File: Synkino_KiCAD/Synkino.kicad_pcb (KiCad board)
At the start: 2 copper layers, 88.4 x 82.3 mm, 180 parts, among them J1 Conn_01x02_Male, J10 EYE8_OUT, J11 EYE4_OUT, J12 2.5mm, J13 EYE5_OUT, J2 2.5mm, J3 3.5mm, J4 Micro_SD_Card_Det_Hirose_DM3AT, J5 EYE1_OUT, J6 EYE6_OUT, J7 EYE2_OUT, J8 EYE7_OUT, J9 EYE3_OUT, Q1 IRF7319, Q2 BC847, SW1 SW_Push, SW2 Rotary_Encoder_Switch, SW3 SW_Push, U1 MCP1702T-5002E/MB, U10 ATMEGA328P-AU, U11 QRE1113, U12 QRE1113, U13 QRE1113, U14 QRE1113, U15 QRE1113, U16 QRE1113, U18 QRE1113, U2 ATMEGA328P-AU, U3 74HC4050, U4 SPIOLED128x64, U5 AP7312-1833W6-7, U6 74HC14, U7 VS1053B, U8 MAX4741, U9 QRE1113, X1 FTDIconn, X2 ICSP, X3 FTDIconn, X4 ICSP, Y1 16Mhz, Y2 12.288MHz, Y3 16Mhz

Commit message: Beautification
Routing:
- net GND: track 176.0 -> 174.2 mm
- net +5V: track 283.3 -> 282.3 mm
- net +3V3: track 220.5 -> 219.8 mm

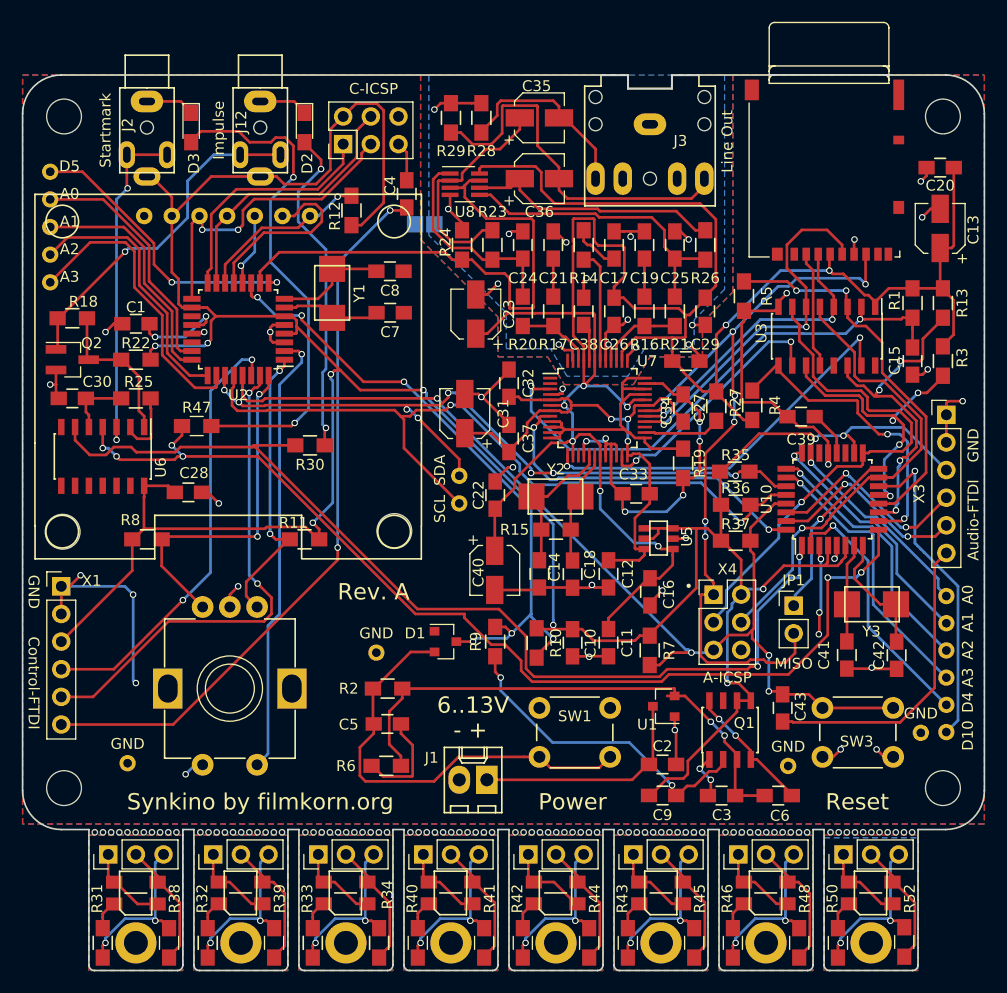
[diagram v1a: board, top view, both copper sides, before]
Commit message: Fixed the U1 footprint
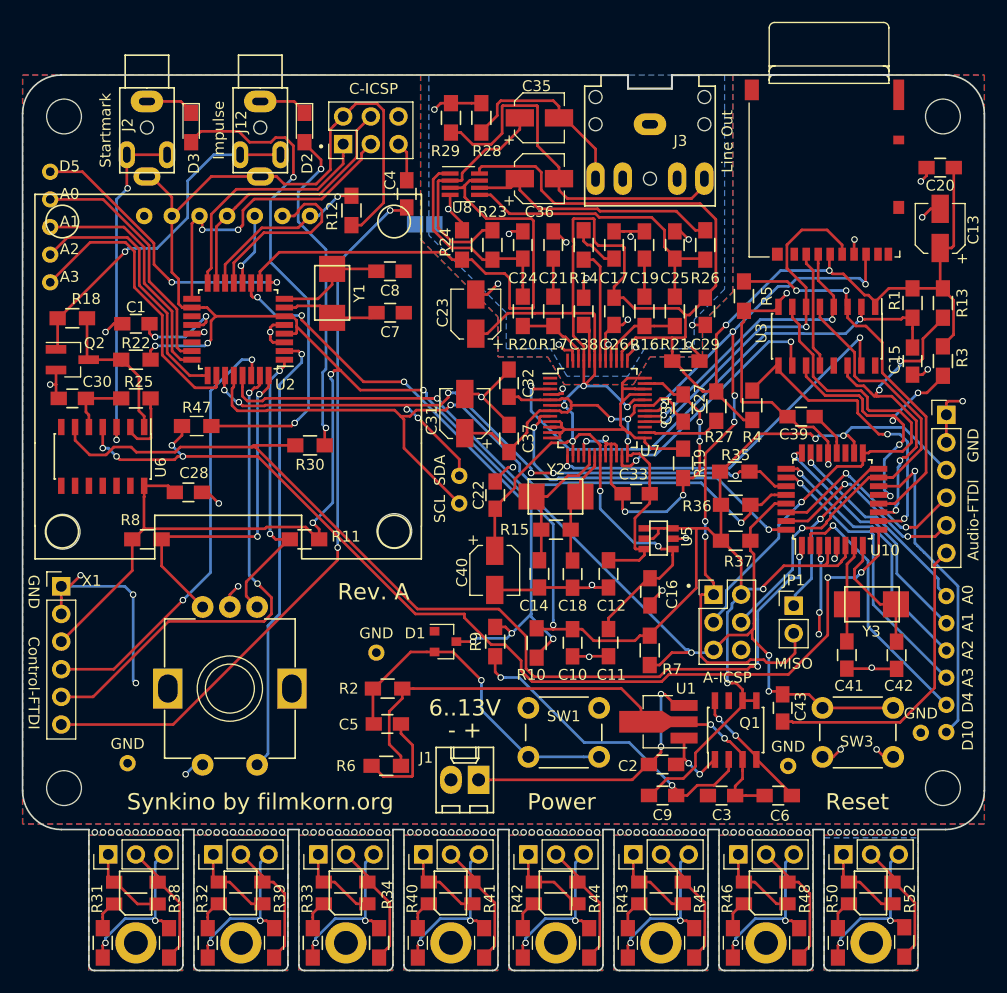
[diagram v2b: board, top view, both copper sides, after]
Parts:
- U1: footprint TO_SOT_Packages_SMD:SOT-23 -> TO_SOT_Packages_SMD:SOT-89-3_Handsoldering
- moved U1 1.43 mm to (130.4, 97.5)
- moved SW1 1.02 mm to (118.1, 96.3)
- moved J1 0.76 mm to (113.5, 102.9)
- moved Q1 0.51 mm to (137.2, 98.3)
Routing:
- net Net-(C5-Pad2): track 40.7 -> 31.2 mm, vias 0 -> 1
- net Net-(C2-Pad1): track 21.1 -> 25.7 mm, vias 0 -> 2
- net GND: track 174.2 -> 171.0 mm, vias 40 -> 39
- net Net-(C3-Pad2): track 49.3 -> 51.2 mm
- net Net-(C6-Pad1): track 12.7 -> 11.6 mm

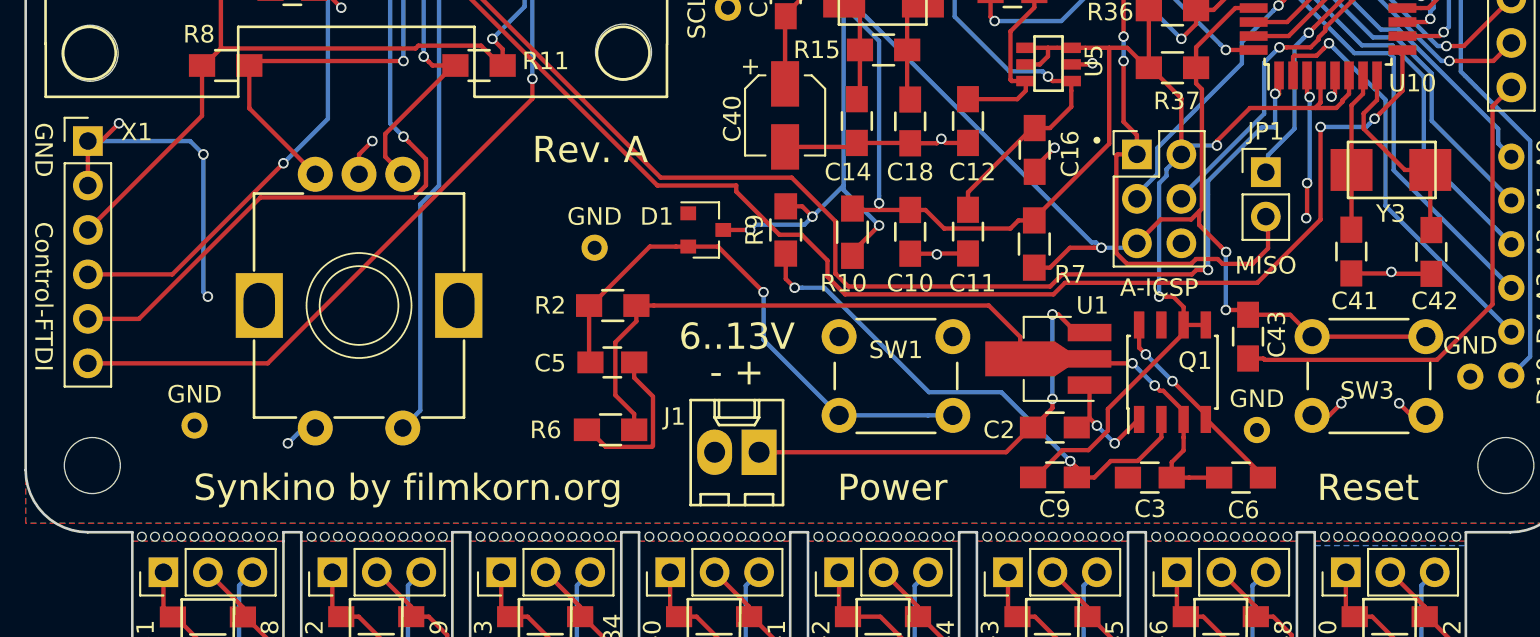
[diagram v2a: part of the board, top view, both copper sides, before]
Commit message: Making Power button bigger
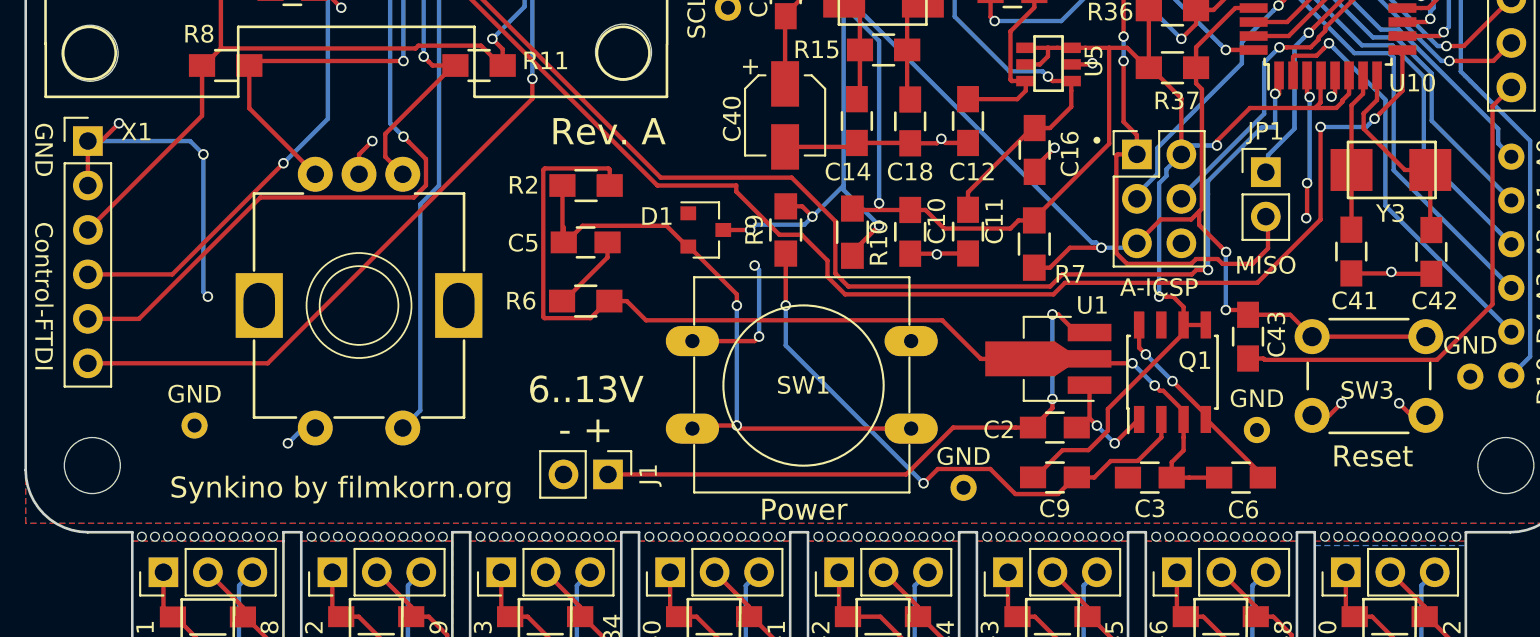
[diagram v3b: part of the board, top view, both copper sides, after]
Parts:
- J1: footprint Connectors_Molex:Molex_KK-6410-02_02x2.54mm_Straight -> Pin_Headers:Pin_Header_Straight_1x02_Pitch2.54mm
- SW1: footprint Buttons_Switches_THT:SW_PUSH_6mm_h5mm -> Buttons_Switches_THT:SW_PUSH-12mm
- moved GND 25.2 mm to (125.2, 104.9)
- moved J1 8.73 mm to (104.9, 104.1), turned to 270 degrees
- moved SW1 8.39 mm to (109.7, 96.5)
- moved R6 7.49 mm to (103.6, 94.2)
- moved C5 7.03 mm to (103.6, 90.9)
- moved R2 7.03 mm to (103.7, 87.6)
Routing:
- net Net-(C3-Pad2): track 51.2 -> 61.4 mm
- net Net-(C2-Pad1): track 25.7 -> 35.0 mm
- net GND: track 171.0 -> 179.1 mm, vias 39 -> 41
- net Net-(C5-Pad2): track 31.2 -> 36.2 mm, vias 1 -> 2
- net Net-(C5-Pad1): track 9.41 -> 4.59 mm
- net Net-(C9-Pad2): track 29.9 -> 33.3 mm

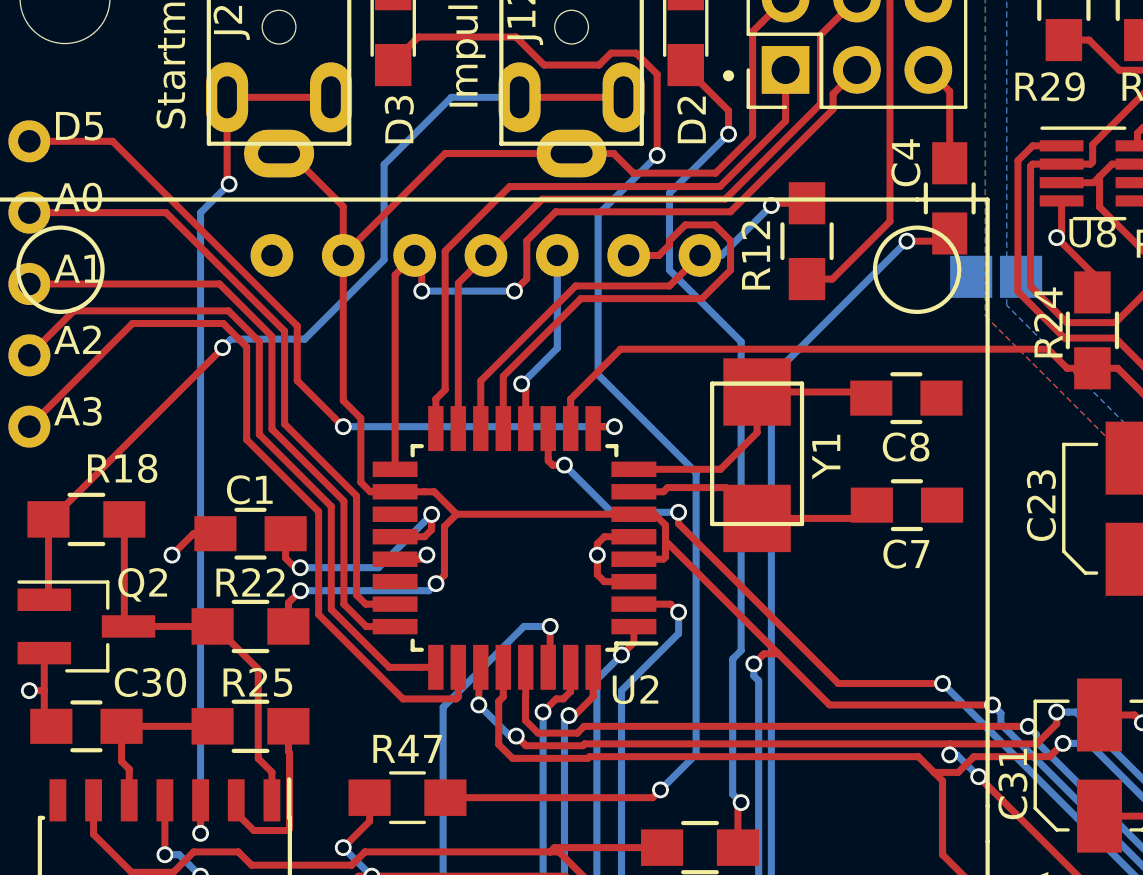
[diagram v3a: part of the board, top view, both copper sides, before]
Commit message: Bit more GND planes
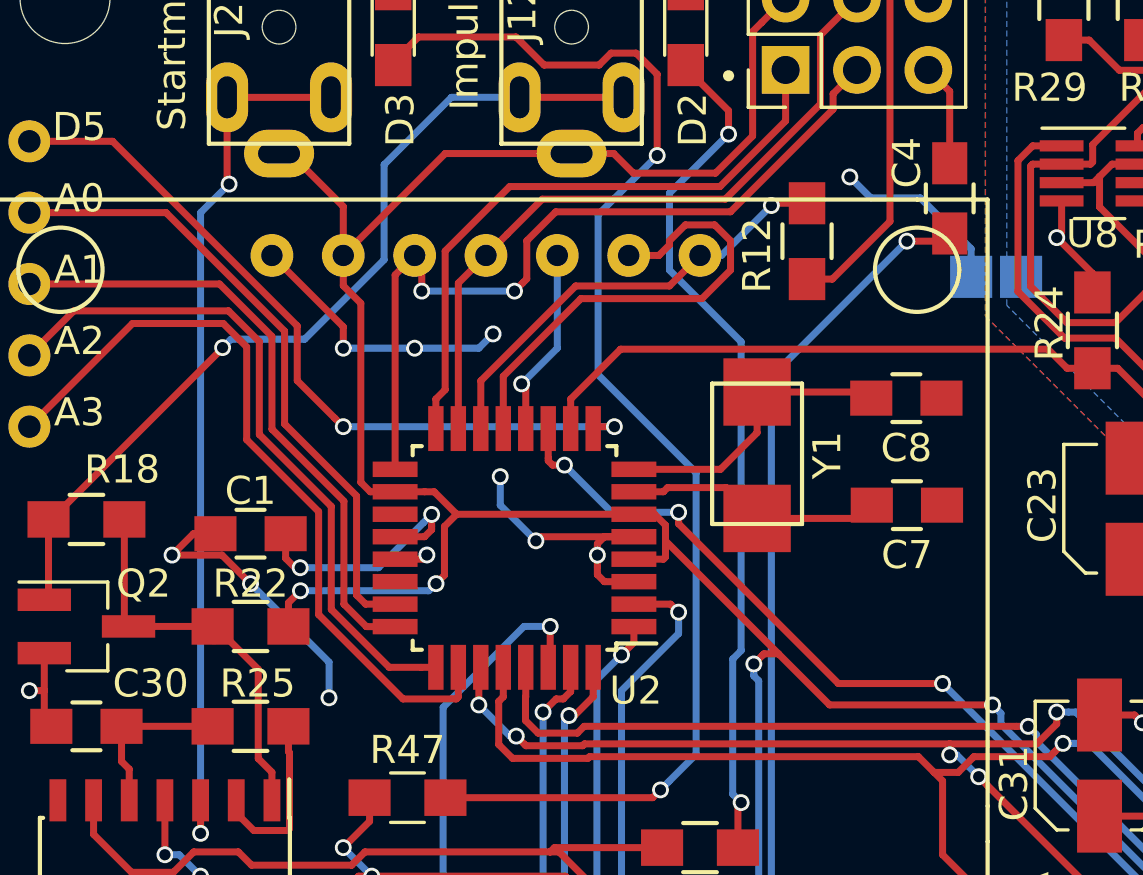
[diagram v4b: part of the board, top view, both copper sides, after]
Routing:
- net GND: track 179.1 -> 210.1 mm, vias 41 -> 49
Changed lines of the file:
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@@
     (links 370)
     (no_connects 0)
-    (area 71.552999 38.024999 160.095001 120.471001)
+    (area 62.682429 32.843999 168.838572 132.270286)
     (thickness 1.6)
     (drawings 81)
-    (tracks 2008)
+    (tracks 2033)
     (zones 0)
     (modules 180)
@@
   (segment (start 83.292 60.96) (end 83.292 61.835) (width 0.25) (layer F.Cu) (net 1))
   (via (at 83.81038 62.171306) (size 0.6) (drill 0.4) (layers F.Cu B.Cu) (net 1))
+  (segment (start 105.885792 49.005792) (end 104.123792 49.005792) (width 0.25) (layer B.Cu) (net 2))
+  (segment (start 104.123792 49.005792) (end 103.378 48.26) (width 0.25) (layer B.Cu) (net 2))
+  (via (at 103.378 48.26) (size 0.6) (drill 0.4) (layers F.Cu B.Cu) (net 2))
+  (segment (start 107.696 51.816) (end 107.696 50.816) (width 0.25) (layer B.Cu) (net 2))
+  (segment (start 107.696 50.816) (end 105.885792 49.005792) (width 0.25) (layer B.Cu) (net 2))
+  (segment (start 87.884 54.356) (end 90.17 54.356) (width 0.25) (layer B.Cu) (net 2))
+  (segment (start 90.17 54.356) (end 90.678 53.848) (width 0.25) (layer B.Cu) (net 2))
+  (via (at 90.678 53.848) (size 0.6) (drill 0.4) (layers F.Cu B.Cu) (net 2))
+  (segment (start 85.344 54.356) (end 87.884 54.356) (width 0.25) (layer B.Cu) (net 2))
+  (via (at 87.884 54.356) (size 0.6) (drill 0.4) (layers F.Cu B.Cu) (net 2))
+  (segment (start 85.344 53.594) (end 85.344 54.356) (width 0.25) (layer F.Cu) (net 2))
+  (segment (start 82.804 51.054) (end 85.344 53.594) (width 0.25) (layer F.Cu) (net 2))
+  (via (at 85.344 54.356) (size 0.6) (drill 0.4) (layers F.Cu B.Cu) (net 2))
+  (segment (start 92.202 61.214) (end 90.932 59.944) (width 0.25) (layer B.Cu) (net 2))
+  (segment (start 90.932 59.944) (end 90.932 58.928) (width 0.25) (layer B.Cu) (net 2))
+  (via (at 90.932 58.928) (size 0.6) (drill 0.4) (layers F.Cu B.Cu) (net 2))
+  (segment (start 95.69 61.068) (end 92.348 61.068) (width 0.25) (layer F.Cu) (net 2))
+  (segment (start 92.348 61.068) (end 92.202 61.214) (width 0.25) (layer F.Cu) (net 2))
+  (via (at 92.202 61.214) (size 0.6) (drill 0.4) (layers F.Cu B.Cu) (net 2))
+  (segment (start 82.042 62.738) (end 84.836 65.532) (width 0.25) (layer B.Cu) (net 2))
+  (via (at 84.836 66.802) (size 0.6) (drill 0.4) (layers F.Cu B.Cu) (net 2))
+  (segment (start 84.836 65.532) (end 84.836 66.802) (width 0.25) (layer B.Cu) (net 2))
+  (segment (start 79.248 61.722) (end 81.026 61.722) (width 0.25) (layer F.Cu) (net 2))
+  (segment (start 81.026 61.722) (end 82.042 62.738) (width 0.25) (layer F.Cu) (net 2))
+  (via (at 82.042 62.738) (size 0.6) (drill 0.4) (layers F.Cu B.Cu) (net 2))
   (segment (start 113.538 96.266) (end 113.538 92.456) (width 0.25) (layer B.Cu) (net 2))
   (segment (start 113.538 92.456) (end 113.284 92.202) (width 0.25) (layer B.Cu) (net 2))
@@
   (segment (start 98.774 58.668) (end 100.076 57.366) (width 0.25) (layer F.Cu) (net 11))
   (segment (start 100.076 57.366) (end 100.076 55.916) (width 0.25) (layer F.Cu) (net 11))
+  (segment (start 86.305645 59.468) (end 87.19 59.468) (width 0.25) (layer F.Cu) (net 12))
+  (segment (start 85.969002 59.131357) (end 86.305645 59.468) (width 0.25) (layer F.Cu) (net 12))
+  (segment (start 85.969002 52.756632) (end 85.969002 59.131357) (width 0.25) (layer F.Cu) (net 12))
+  (segment (start 85.344 52.13163) (end 85.969002 52.756632) (width 0.25) (layer F.Cu) (net 12))
+  (segment (start 85.344 51.054) (end 85.344 52.13163) (width 0.25) (layer F.Cu) (net 12))
   (segment (start 129.196 104.311) (end 129.321 104.311) (width 0.25) (layer F.Cu) (net 12))
   (segment (start 129.321 104.311) (end 130.879001 102.752999) (width 0.25) (layer F.Cu) (net 12))
@@
   (segment (start 102.267001 40.734999) (end 101.941999 41.060001) (width 0.25) (layer F.Cu) (net 12))
   (segment (start 101.941999 41.060001) (end 101.092 41.91) (width 0.25) (layer F.Cu) (net 12))
-  (segment (start 86.305645 59.468) (end 87.19 59.468) (width 0.25) (layer F.Cu) (net 12))
-  (segment (start 85.969002 59.131357) (end 86.305645 59.468) (width 0.25) (layer F.Cu) (net 12))
-  (segment (start 85.344 51.054) (end 85.344 56.224996) (width 0.25) (layer F.Cu) (net 12))
-  (segment (start 85.969002 56.849998) (end 85.969002 59.131357) (width 0.25) (layer F.Cu) (net 12))
-  (segment (start 85.344 56.224996) (end 85.969002 56.849998) (width 0.25) (layer F.Cu) (net 12))
   (segment (start 85.344 51.054) (end 88.972 47.426) (width 0.25) (layer F.Cu) (net 12))
   (segment (start 88.972 47.426) (end 93.472 47.426) (width 0.25) (layer F.Cu) (net 12))
@@
   (segment (start 91.268228 48.60101) (end 98.756405 48.60101) (width 0.25) (layer F.Cu) (net 69))
   (segment (start 88.64 57.218) (end 88.64 56.168) (width 0.25) (layer F.Cu) (net 69))
+  (segment (start 87.19 51.748) (end 87.884 51.054) (width 0.25) (layer F.Cu) (net 70))
+  (segment (start 87.19 58.668) (end 87.19 51.748) (width 0.25) (layer F.Cu) (net 70))
   (segment (start 91.876999 51.887001) (end 91.739999 52.024001) (width 0.25) (layer F.Cu) (net 70))
   (segment (start 91.739999 52.024001) (end 91.44 52.324) (width 0.25) (layer F.Cu) (net 70))
@@
   (via (at 88.138 52.324) (size 0.6) (drill 0.4) (layers F.Cu B.Cu) (net 70))
   (via (at 91.44 52.324) (size 0.6) (drill 0.4) (layers F.Cu B.Cu) (net 70))
-  (segment (start 87.19 58.668) (end 87.19 51.748) (width 0.25) (layer F.Cu) (net 70))
-  (segment (start 87.19 51.748) (end 87.884 51.054) (width 0.25) (layer F.Cu) (net 70))
   (segment (start 92.71 64.262) (end 92.71 65.648) (width 0.25) (layer F.Cu) (net 73))
   (segment (start 92.71 65.648) (end 92.64 65.718) (width 0.25) (layer F.Cu) (net 73))
